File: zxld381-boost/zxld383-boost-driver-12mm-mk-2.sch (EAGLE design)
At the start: 5 parts, among them Q1 MOSFET-NCHANNELIRLML2502

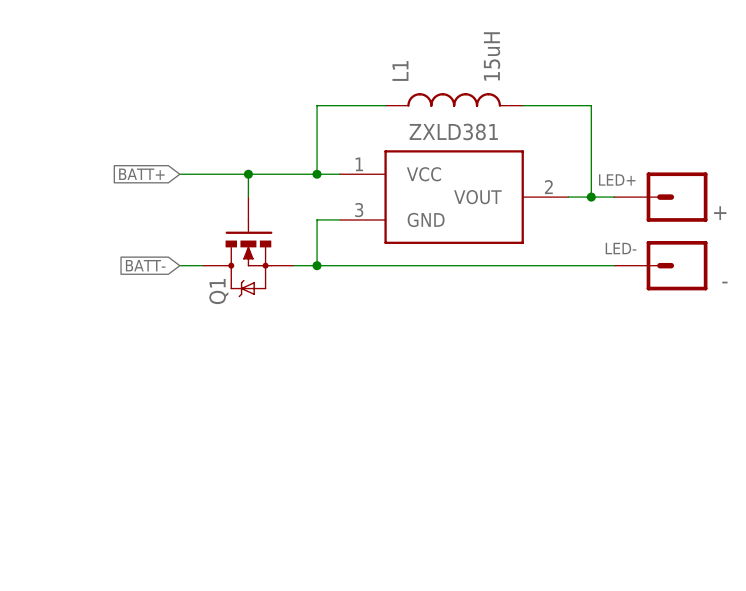
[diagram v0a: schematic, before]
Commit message: bunch of new zxld38' boards and a third revision of the lm3410 pcb
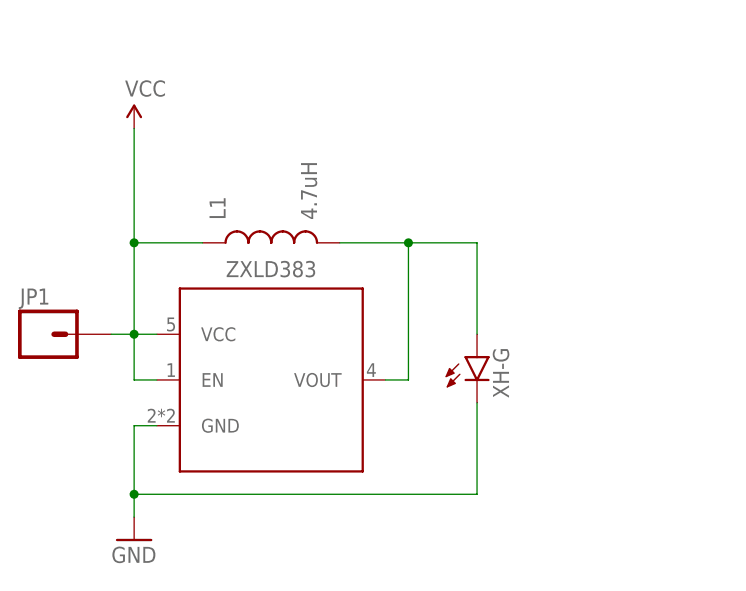
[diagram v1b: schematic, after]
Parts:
- removed +, -: M01PTH-NS-NOTSUCK, A_butts:M01PTH-NS-NOTSUCK
- removed Q1: MOSFET-NCHANNELIRLML2502, A_butts:MOSFET-NCHANNELIRLML2502
- removed ZXLD381: ZXLD381, A_butts:ZXLD381
- added JP1: M01NOT-A-VIA-NOPE, A_butts:M01NOT-A-VIA-NOPE
- added XH-G: LEDXH-G, A_butts:LEDXH-G
- added ZXLD383: ZXLD383, A_butts:ZXLD383
- L1: value 15uH -> 4.7uH; device A_butts:INDUCTOR0805 -> A_butts:INDUCTOR1007
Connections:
- removed net BATT+: L1.1, Q1.G, ZXLD381.VCC
- removed net BATT-: Q1.D
- removed net LED+: +.1, L1.2, ZXLD381.VOUT
- removed net LED-: -.1, Q1.S, ZXLD381.GND
- new net GND: XH-G.C, ZXLD383.GND
- new net VCC: JP1.1, L1.1, ZXLD383.EN, ZXLD383.VCC
- new net VOUT: L1.2, XH-G.A, ZXLD383.VOUT
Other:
- moved on the sheet: L1
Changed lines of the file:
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@@
 </classes>
 <parts>
-<part name="ZXLD381" library="A_butts" deviceset="ZXLD381" device=""/>
-<part name="+" library="A_butts" deviceset="M01" device="PTH-NS-NOTSUCK" value="M01PTH-NS-NOTSUCK"/>
-<part name="-" library="A_butts" deviceset="M01" device="PTH-NS-NOTSUCK" value="M01PTH-NS-NOTSUCK"/>
-<part name="L1" library="A_butts" deviceset="INDUCTOR" device="0805" value="15uH"/>
-<part name="Q1" library="A_butts" deviceset="MOSFET-NCHANNEL" device="IRLML2502" value="MOSFET-NCHANNELIRLML2502"/>
+<part name="SUPPLY1" library="A_butts" deviceset="VCC" device=""/>
+<part name="GND1" library="A_butts" deviceset="GND" device=""/>
+<part name="L1" library="A_butts" deviceset="INDUCTOR" device="1007" value="4.7uH"/>
+<part name="ZXLD383" library="A_butts" deviceset="ZXLD383" device=""/>
+<part name="JP1" library="A_butts" deviceset="M01" device="NOT-A-VIA-NOPE"/>
+<part name="XH-G" library="A_butts" deviceset="LED" device="XH-G" value="LEDXH-G"/>
 </parts>
 <sheets>
@@
 </plain>
 <instances>
-<instance part="ZXLD381" gate="U$1" x="50.8" y="43.18"/>
-<instance part="+" gate="G$1" x="76.2" y="43.18" smashed="yes" rot="R180">
-<attribute name="NAME" x="81.28" y="42.418" size="1.778" layer="95" rot="R180"/>
-</instance>
-<instance part="-" gate="G$1" x="76.2" y="35.56" smashed="yes" rot="R180">
-<attribute name="NAME" x="81.28" y="34.798" size="1.778" layer="95" rot="R180"/>
-</instance>
-<instance part="L1" gate="G$1" x="50.8" y="53.34" rot="R90"/>
-<instance part="Q1" gate="G$1" x="27.94" y="35.56" rot="MR270"/>
+<instance part="SUPPLY1" gate="G$1" x="15.24" y="50.8"/>
+<instance part="GND1" gate="1" x="15.24" y="5.08"/>
+<instance part="L1" gate="G$1" x="30.48" y="38.1" rot="R90"/>
+<instance part="ZXLD383" gate="G$1" x="30.48" y="22.86"/>
+<instance part="JP1" gate="G$1" x="5.08" y="27.94"/>
+<instance part="XH-G" gate="G$1" x="53.34" y="25.4"/>
 </instances>
 <busses>
 </busses>
 <nets>
-<net name="LED+" class="0">
+<net name="VCC" class="0">
 <segment>
-<pinref part="ZXLD381" gate="U$1" pin="VOUT"/>
-<wire x1="63.5" y1="43.18" x2="66.04" y2="43.18" width="0.1524" layer="91"/>
-<wire x1="66.04" y1="43.18" x2="66.04" y2="53.34" width="0.1524" layer="91"/>
-<pinref part="L1" gate="G$1" pin="2"/>
-<wire x1="66.04" y1="53.34" x2="58.42" y2="53.34" width="0.1524" layer="91"/>
-<pinref part="+" gate="G$1" pin="1"/>
-<wire x1="68.58" y1="43.18" x2="66.04" y2="43.18" width="0.1524" layer="91"/>
-<junction x="66.04" y="43.18"/>
-<label x="71.12" y="45.72" size="1.27" layer="95" rot="R180"/>
+<pinref part="ZXLD383" gate="G$1" pin="EN"/>
+<pinref part="SUPPLY1" gate="G$1" pin="VCC"/>
+<wire x1="15.24" y1="38.1" x2="15.24" y2="50.8" width="0.1524" layer="91"/>
+<pinref part="L1" gate="G$1" pin="1"/>
+<wire x1="22.86" y1="38.1" x2="15.24" y2="38.1" width="0.1524" layer="91"/>
+<junction x="15.24" y="38.1"/>
+<wire x1="15.24" y1="27.94" x2="15.24" y2="38.1" width="0.1524" layer="91"/>
+<pinref part="ZXLD383" gate="G$1" pin="VCC"/>
+<wire x1="17.78" y1="27.94" x2="15.24" y2="27.94" width="0.1524" layer="91"/>
+<junction x="15.24" y="27.94"/>
+<wire x1="15.24" y1="27.94" x2="15.24" y2="22.86" width="0.1524" layer="91"/>
+<wire x1="15.24" y1="22.86" x2="17.78" y2="22.86" width="0.1524" layer="91"/>
+<pinref part="JP1" gate="G$1" pin="1"/>
+<wire x1="12.7" y1="27.94" x2="15.24" y2="27.94" width="0.1524" layer="91"/>
 </segment>
 </net>
-<net name="LED-" class="0">
+<net name="GND" class="0">
 <segment>
-<pinref part="Q1" gate="G$1" pin="S"/>
-<wire x1="33.02" y1="35.56" x2="35.56" y2="35.56" width="0.1524" layer="91"/>
-<wire x1="35.56" y1="35.56" x2="35.56" y2="40.64" width="0.1524" layer="91"/>
-<pinref part="ZXLD381" gate="U$1" pin="GND"/>
-<wire x1="35.56" y1="40.64" x2="38.1" y2="40.64" width="0.1524" layer="91"/>
-<junction x="35.56" y="35.56"/>
-<wire x1="35.56" y1="35.56" x2="68.58" y2="35.56" width="0.1524" layer="91"/>
-<pinref part="-" gate="G$1" pin="1"/>
-<label x="71.12" y="38.1" size="1.27" layer="95" rot="R180"/>
+<pinref part="GND1" gate="1" pin="GND"/>
+<pinref part="ZXLD383" gate="G$1" pin="GND"/>
+<wire x1="17.78" y1="17.78" x2="15.24" y2="17.78" width="0.1524" layer="91"/>
+<wire x1="15.24" y1="17.78" x2="15.24" y2="10.16" width="0.1524" layer="91"/>
+<pinref part="XH-G" gate="G$1" pin="C"/>
+<wire x1="15.24" y1="10.16" x2="15.24" y2="7.62" width="0.1524" layer="91"/>
+<wire x1="15.24" y1="10.16" x2="53.34" y2="10.16" width="0.1524" layer="91"/>
+<wire x1="53.34" y1="10.16" x2="53.34" y2="20.32" width="0.1524" layer="91"/>
+<junction x="15.24" y="10.16"/>
 </segment>
 </net>
-<net name="BATT+" class="0">
+<net name="VOUT" class="0">
 <segment>
-<pinref part="ZXLD381" gate="U$1" pin="VCC"/>
-<pinref part="L1" gate="G$1" pin="1"/>
-<wire x1="35.56" y1="45.72" x2="38.1" y2="45.72" width="0.1524" layer="91"/>
-<wire x1="43.18" y1="53.34" x2="35.56" y2="53.34" width="0.1524" layer="91"/>
-<wire x1="35.56" y1="53.34" x2="35.56" y2="45.72" width="0.1524" layer="91"/>
-<pinref part="Q1" gate="G$1" pin="G"/>
-<wire x1="27.94" y1="43.18" x2="27.94" y2="45.72" width="0.1524" layer="91"/>
-<wire x1="27.94" y1="45.72" x2="35.56" y2="45.72" width="0.1524" layer="91"/>
-<junction x="35.56" y="45.72"/>
-<wire x1="27.94" y1="45.72" x2="20.32" y2="45.72" width="0.1524" layer="91"/>
-<junction x="27.94" y="45.72"/>
-<label x="20.32" y="45.72" size="1.27" layer="95" rot="R180" xref="yes"/>
+<pinref part="ZXLD383" gate="G$1" pin="VOUT"/>
+<wire x1="43.18" y1="22.86" x2="45.72" y2="22.86" width="0.1524" layer="91"/>
+<pinref part="L1" gate="G$1" pin="2"/>
+<wire x1="38.1" y1="38.1" x2="45.72" y2="38.1" width="0.1524" layer="91"/>
+<wire x1="45.72" y1="22.86" x2="45.72" y2="38.1" width="0.1524" layer="91"/>
+<wire x1="45.72" y1="38.1" x2="53.34" y2="38.1" width="0.1524" layer="91"/>
+<junction x="45.72" y="38.1"/>
+<pinref part="XH-G" gate="G$1" pin="A"/>
+<wire x1="53.34" y1="38.1" x2="53.34" y2="27.94" width="0.1524" layer="91"/>
 </segment>
 </net>
-<net name="BATT-" class="0">
-<segment>
-<pinref part="Q1" gate="G$1" pin="D"/>
-<wire x1="22.86" y1="35.56" x2="20.32" y2="35.56" width="0.1524" layer="91"/>
-<label x="20.32" y="35.56" size="1.27" layer="95" rot="R180" xref="yes"/>
-</segment>
-</net>
